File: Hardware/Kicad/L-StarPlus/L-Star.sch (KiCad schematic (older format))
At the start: 51 parts, among them IC1 24LC512, IC2 AS6C1008-55PCN, IC3 WDC 65C02, IC4 P8X32A, IC5 LM1086-5.0, IC6 LM1086-3.3, P1 PROP PLUG, P2 EXPANSION, P3 PS/2 KBD, P4 RESET, P5 RESET6502, P6 VIDEO OUT, P7 7-15V 1-1.5A IN, SW1 RESET, SW2 RESET6502, SW3 OFF - ON, U1 OSHW Logo, U2 Mount hole, U3 Mount hole, U4 Mount hole, X1 5MHz

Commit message: Fixed jumpers, added Reset, moved LED
I inadvertently put ~RAMEN on the wrong jumper in Rev2 (J2 instead of J4) so it was impossible to have keyboard, video and SRAM. This moves ~RAMEN to J4 and A16 to J2.
Also added ~RESET6502 to the jumpers to make it possible to connect a Propeller pin to it
There was not enough space around the RESET6502 button in Rev2 so I moved the LED to make space. I also moved both pushbutton switches to be parallel and centered between surrounding parts.
Also some more minor modifications to PCB and schematic.
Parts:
- IC3: value WDC 65C02 -> W65C02S6TPG-14
- JP1, JP3, JP5: footprint Pin_Headers:Pin_Header_Straight_1x07 -> 00Jac:00JG-Pin_Header_Straight_1x08; symbol CONN_01X07 -> CONN_01X08
- JP2: value RDY/~SO~/~SYNC~/~NMI~/~IRQ~/~RAMEN~/+ -> RDY/~SO~/~SYNC~/~NMI~/~IRQ~/~RES~/A16/GND; footprint Pin_Headers:Pin_Header_Straight_1x07 -> 00Jac:00JG-Pin_Header_Straight_1x08; symbol CONN_01X07 -> CONN_01X08
- JP4: value RDY/~SO~/~SYNC~/~NMI~/~IRQ~/A16/GND -> RDY/~SO~/~SYNC~/~NMI~/~IRQ~/~RES~/~RAM~/+3.3; footprint Pin_Headers:Pin_Header_Straight_1x07 -> 00Jac:00JG-Pin_Header_Straight_1x08; symbol CONN_01X07 -> CONN_01X08
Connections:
- net +3V3: now also JP4.1 (P1); no longer JP2.1 (P1)
- net A16: now also JP2.2 (P2); no longer JP4.2 (P2)
- net GND: now also JP2.1 (P1); no longer JP4.1 (P1)
- net P25: now also JP1.8 (P8)
- net P26: now also JP3.8 (P8)
- net P27: now also JP5.8 (P8)
- net RDY: now also JP2.8 (P8), JP4.8 (P8); no longer JP2.7 (P7), JP4.7 (P7)
- net ~IRQ: now also JP2.4 (P4), JP4.4 (P4); no longer JP2.3 (P3), JP4.3 (P3)
- net ~NMI: now also JP2.5 (P5), JP4.5 (P5); no longer JP2.4 (P4), JP4.4 (P4)
- net ~RAMEN: now also JP4.2 (P2); no longer JP2.2 (P2)
- net ~RES6502: now also JP2.3 (P3), JP4.3 (P3)
- net ~SO: now also JP2.7 (P7), JP4.7 (P7); no longer JP2.6 (P6), JP4.6 (P6)
- net ~SYNC: now also JP2.6 (P6), JP4.6 (P6); no longer JP2.5 (P5), JP4.5 (P5)

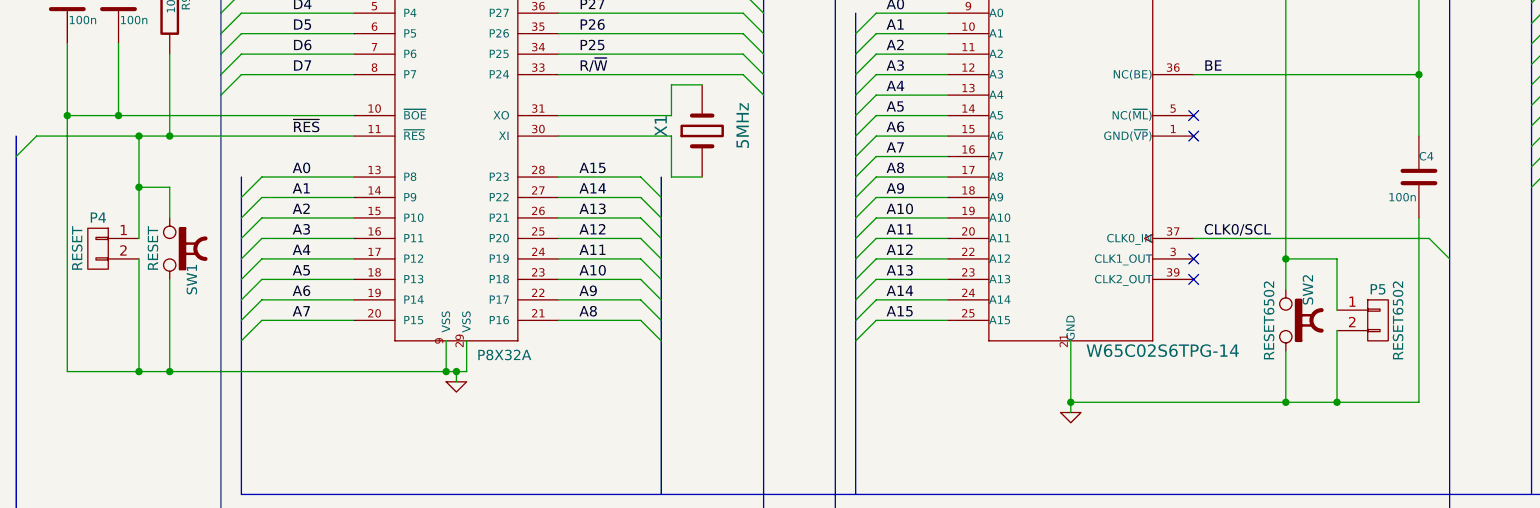
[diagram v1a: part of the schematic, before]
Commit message: Rev 3 Finished
Made all the soldering pads a little bigger, and made the pads for the voltage regulators a little smaller to leave more room for the switch. Many more small tweaks to footprints and PCB.
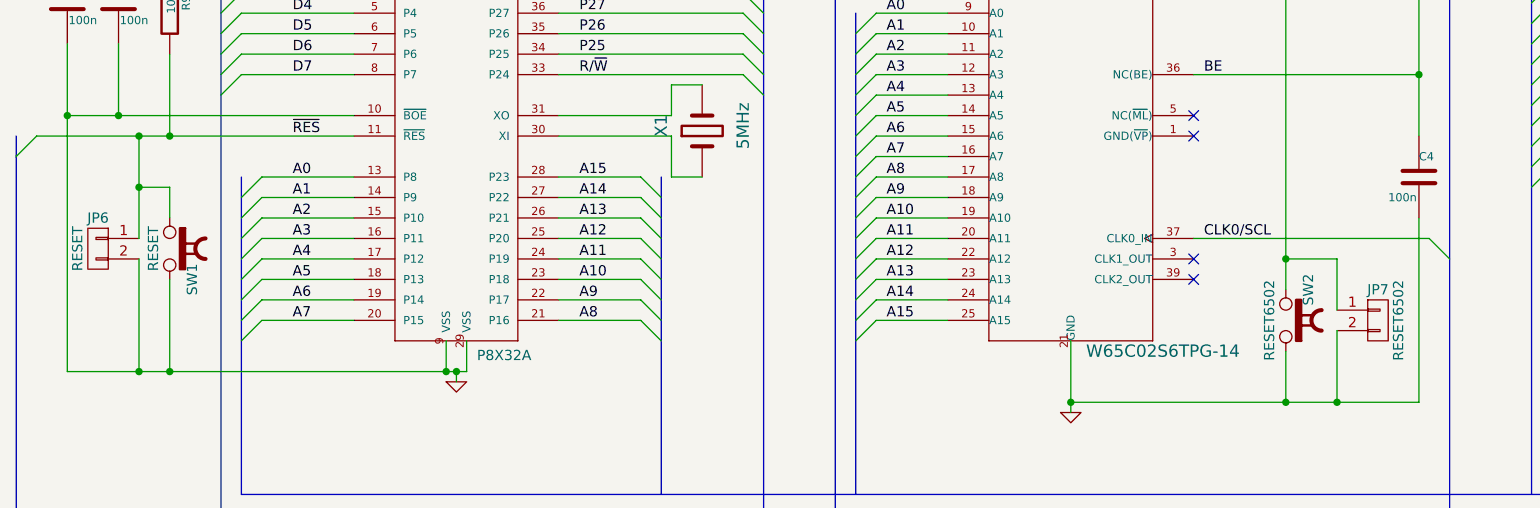
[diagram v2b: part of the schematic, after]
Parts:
- C7, C8, C9: footprint Discret:C1V7 -> 00Jac:00JG-C1V5
- IC1: footprint Sockets_DIP:DIP-8__300 -> 00Jac:00JG-DIP-8__300
- IC2: footprint Sockets_DIP:DIP-32__600 -> 00Jac:00JG-DIP-32__600
- IC3, IC4: footprint Sockets_DIP:DIP-40__600 -> 00Jac:00JG-DIP-40__600
- JP6: renamed from P4; footprint Pin_Headers:Pin_Header_Straight_1x02 -> 00Jac:00JG-Pin_Header_Straight_1x02
- JP7: renamed from P5; footprint Pin_Headers:Pin_Header_Straight_1x02 -> 00Jac:00JG-Pin_Header_Straight_1x02
- P1: footprint Pin_Headers:Pin_Header_Angled_1x04 -> 00Jac:00JG-Pin_Header_Angled_1x04
- P2: footprint Pin_Headers:Pin_Header_Straight_2x20 -> 00Jac:00JG-Pin_Header_Straight_2x20
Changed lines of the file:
@@
 F 0 "P1" V 12750 4300 50  0000 C CNN
 F 1 "PROP PLUG" V 12950 4300 50  0000 C CNN
-F 2 "Pin_Headers:Pin_Header_Angled_1x04" H 12800 4300 60  0001 C CNN
+F 2 "00Jac:00JG-Pin_Header_Angled_1x04" H 12800 4300 60  0001 C CNN
 F 3 "~" H 12800 4300 60  0000 C CNN
 	1    12800 4300
@@
 F 0 "C7" H 5250 9400 50  0000 L CNN
 F 1 "47u/16V" H 5250 9150 50  0000 L CNN
-F 2 "Discret:C1V7" H 5200 9300 60  0001 C CNN
+F 2 "00Jac:00JG-C1V5" H 5200 9300 60  0001 C CNN
 F 3 "~" H 5200 9300 60  0000 C CNN
 	1    5200 9300
@@
 F 0 "C8" H 6150 9400 50  0000 L CNN
 F 1 "47u/16V" H 6150 9150 50  0000 L CNN
-F 2 "Discret:C1V7" H 6100 9300 60  0001 C CNN
+F 2 "00Jac:00JG-C1V5" H 6100 9300 60  0001 C CNN
 F 3 "~" H 6100 9300 60  0000 C CNN
 	1    6100 9300
@@
 F 0 "C9" H 7050 9400 50  0000 L CNN
 F 1 "47u/16V" H 7050 9150 50  0000 L CNN
-F 2 "Discret:C1V7" H 7000 9300 60  0001 C CNN
+F 2 "00Jac:00JG-C1V5" H 7000 9300 60  0001 C CNN
 F 3 "~" H 7000 9300 60  0000 C CNN
 	1    7000 9300
@@
 F 0 "IC4" H 2650 6650 50  0000 L BNN
 F 1 "P8X32A" H 3050 4400 50  0000 L BNN
-F 2 "Sockets_DIP:DIP-40__600" H 2950 5550 50  0001 C CNN
+F 2 "00Jac:00JG-DIP-40__600" H 2950 5550 50  0001 C CNN
 F 3 "~" H 3100 5300 60  0000 C CNN
 	1    2950 5550
@@
 F 0 "IC1" H 2750 3000 60  0000 C CNN
 F 1 "24LC512" H 3150 2300 60  0000 C CNN
-F 2 "Sockets_DIP:DIP-8__300" H 2950 2650 60  0001 C CNN
+F 2 "00Jac:00JG-DIP-8__300" H 2950 2650 60  0001 C CNN
 F 3 "" H 2950 2650 60  0000 C CNN
 	1    2950 2650
@@
 F 0 "IC3" H 5600 6650 60  0000 C CNN
 F 1 "W65C02S6TPG-14" H 6400 3950 60  0000 C CNN
-F 2 "Sockets_DIP:DIP-40__600" H 5250 6850 60  0001 C CNN
+F 2 "00Jac:00JG-DIP-40__600" H 5250 6850 60  0001 C CNN
 F 3 "~" H 5950 5300 60  0000 C CNN
 	1    5950 5300
@@
 F 0 "IC2" H 8750 5875 50  0000 L BNN
 F 1 "AS6C1008-55PCN" H 8400 3950 50  0000 L BNN
-F 2 "Sockets_DIP:DIP-32__600" H 9150 4950 50  0001 C CNN
+F 2 "00Jac:00JG-DIP-32__600" H 9150 4950 50  0001 C CNN
 F 3 "" H 9150 4950 60  0000 C CNN
 	1    9150 4950
@@
 F 0 "P2" H 14500 6450 50  0000 C CNN
 F 1 "EXPANSION" V 14500 5400 50  0000 C CNN
-F 2 "Pin_Headers:Pin_Header_Straight_2x20" H 14500 4450 60  0001 C CNN
+F 2 "00Jac:00JG-Pin_Header_Straight_2x20" H 14500 4450 60  0001 C CNN
 F 3 "" H 14500 4450 60  0000 C CNN
 	1    14500 5400
@@
 $EndComp
 $Comp
-L CONN_01X02 P5
+L CONN_01X02 JP7
 U 1 1 54CD3D2C
 P 7450 6500
-F 0 "P5" H 7450 6650 50  0000 C CNN
+F 0 "JP7" H 7450 6650 50  0000 C CNN
 F 1 "RESET6502" V 7550 6500 50  0000 C CNN
-F 2 "Pin_Headers:Pin_Header_Straight_1x02" H 7450 6500 60  0001 C CNN
+F 2 "00Jac:00JG-Pin_Header_Straight_1x02" H 7450 6500 60  0001 C CNN
 F 3 "" H 7450 6500 60  0000 C CNN
 	1    7450 6500
@@
 $EndComp
 $Comp
-L CONN_01X02 P4
+L CONN_01X02 JP6
 U 1 1 54CD4BD6
 P 1200 6150
-F 0 "P4" H 1200 6300 50  0000 C CNN
+F 0 "JP6" H 1200 6300 50  0000 C CNN
 F 1 "RESET" V 1300 6150 50  0000 C CNN
-F 2 "Pin_Headers:Pin_Header_Straight_1x02" H 1200 6150 60  0001 C CNN
+F 2 "00Jac:00JG-Pin_Header_Straight_1x02" H 1200 6150 60  0001 C CNN
 F 3 "" H 1200 6150 60  0000 C CNN
 	1    1200 6150

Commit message: Rev.4 schematic and PCB
Replaced the expansion connector by a 50-pin header so I could add all the signals including BE (I added a pull-up resistor for the BE pin). It's even possible to replicate the entire jumper block on an expension board or an external connector now. Another possibility is to cut off the entire right side of the board (with all the connections and the jumper block) or leave it unpopulated, and make the necessary connections via the expansion port. The new connector is backwards compatible with the old one from the Rev.1, Rev.2 and Rev.3 boards.

Rewired almost the entire board to make it smaller again; I finally got it to fit into slightly over 80x100mm (you'll have to cut a small sliver off the top or bottom to make it fit completely)

For this, I slightly reduced the size of the TO220 pads for the voltage regulators.

Also fixed a small problem in the mini-din 6 footprint: the shield is now grounded.
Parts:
- added R16: 3K3, 00Jac:00JG-R400, symbol R
- P2: footprint 00Jac:00JG-Pin_Header_Straight_2x20 -> Pin_Headers:Pin_Header_Straight_2x25; symbol CONN_02X20 -> CONN_02X25
- P7: value 7-15V 1-1.5A IN -> 7-15V 1.5A IN
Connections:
- net +3V3: now also P2.9 (P9), R16.1; no longer IC3.36 (NC(BE)), P2.1 (P1)
- net +5V: now also P2.11 (P11); no longer P2.3 (P3)
- net A0: now also P2.33 (P33); no longer P2.25 (P25)
- net A1: now also P2.35 (P35); no longer P2.27 (P27)
- net A10: now also IC2.27 (A8), P2.44 (P44); no longer IC2.28 (A13), P2.36 (P36)
- net A11: now also IC2.28 (A13), P2.42 (P42); no longer IC2.23 (A10), P2.34 (P34)
- net A12: now also IC2.26 (A9), P2.40 (P40); no longer IC2.27 (A8), P2.32 (P32)
- net A13: now also IC2.25 (A11), P2.38 (P38); no longer IC2.26 (A9), P2.30 (P30)
- net A14: now also IC2.23 (A10), P2.36 (P36); no longer IC2.25 (A11), P2.28 (P28)
- net A15: now also P2.34 (P34); no longer P2.26 (P26)
- net A16: now also P2.1 (P1)
- net A2: now also P2.37 (P37); no longer P2.29 (P29)
- net A3: now also P2.39 (P39); no longer P2.31 (P31)
- net A4: now also P2.41 (P41); no longer P2.33 (P33)
- net A5: now also P2.43 (P43); no longer P2.35 (P35)
- net A6: now also P2.45 (P45); no longer P2.37 (P37)
- net A7: now also P2.47 (P47); no longer P2.39 (P39)
- net A8: now also P2.48 (P48); no longer P2.40 (P40)
- net A9: now also P2.46 (P46); no longer P2.38 (P38)
- net CLK0/SCL: now also P2.24 (P24); no longer P2.16 (P16)
- net D0: now also P2.17 (P17); no longer P2.9 (P9)
- net D1: now also IC2.14 (DQ1), P2.19 (P19); no longer IC2.17 (DQ3), P2.11 (P11)
- net D2: now also IC2.13 (DQ0), P2.21 (P21); no longer IC2.14 (DQ1), P2.13 (P13)
- net D3: now also IC2.17 (DQ3), P2.23 (P23); no longer IC2.13 (DQ0), P2.15 (P15)
- net D4: now also P2.25 (P25); no longer P2.17 (P17)
- net D5: now also P2.27 (P27); no longer P2.19 (P19)
- net D6: now also P2.29 (P29); no longer P2.21 (P21)
- net D7: now also P2.31 (P31); no longer P2.23 (P23)
- net GND: now also P2.10 (P10), P2.49 (P49), P2.50 (P50); no longer P2.2 (P2)
- net KBCLK: now also P2.4 (P4)
- net KBDATA: now also P2.6 (P6)
- net P25: now also P2.30 (P30); no longer P2.22 (P22)
- net P26: now also P2.28 (P28); no longer P2.20 (P20)
- net P27: now also P2.26 (P26); no longer P2.18 (P18)
- net P30: now also P2.20 (P20); no longer P2.12 (P12)
- net P31: now also P2.18 (P18); no longer P2.10 (P10)
- net R/~W: now also P2.32 (P32); no longer P2.24 (P24)
- net RDY: now also P2.7 (P7)
- net SDA: now also P2.22 (P22); no longer P2.14 (P14)
- net TVOUT: now also P2.8 (P8)
- net ~IRQ: now also P2.14 (P14); no longer P2.6 (P6)
- net ~NMI: now also P2.13 (P13); no longer P2.5 (P5)
- net ~RAMEN: now also P2.3 (P3)
- net ~RES: now also P2.2 (P2)
- net ~RES6502: now also P2.12 (P12); no longer P2.4 (P4)
- net ~SO: now also P2.15 (P15); no longer P2.7 (P7)
- net ~SYNC: now also P2.16 (P16); no longer P2.8 (P8)
- new net BE: IC3.36 (NC(BE)), P2.5 (P5), R16.2
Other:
- moved on the sheet: C6

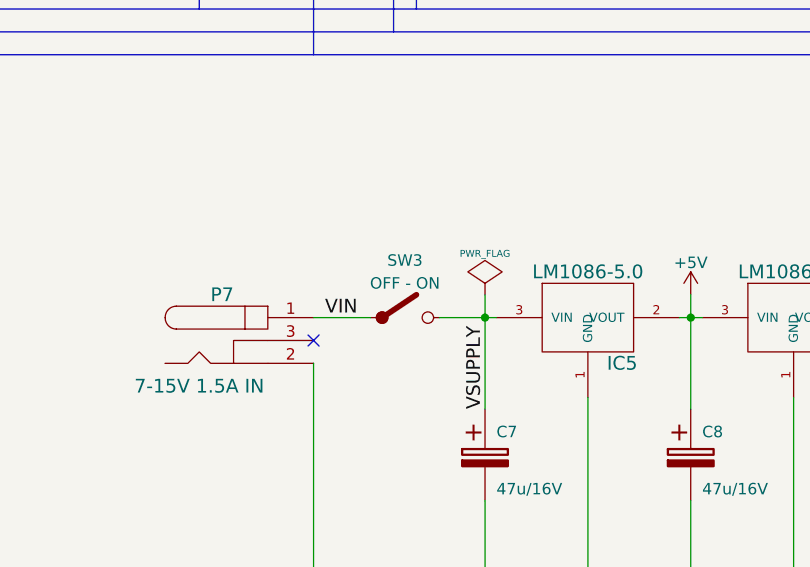
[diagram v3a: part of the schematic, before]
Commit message: PCB Revision 5
I had Rev 4 manufactured at OSHPark and ran into the following problems:
1. The pad-to-soldermask clearance was too big (.0078 inches) so the copper of the flood planes was exposed
2. The flood plane clearance was too small so in combination with the above, it was too easy to short pads to flood planes
3. In a few places, parts were too close together, which also made it too easy to cause short circuits
4. Some vias didn't get drilled because apparently the drill bit broke while the factory was processing my board
5. I had moved the mounting hole on the bottom left under the SRAM chip but that really wasn't a good location

To fix this, I made the following changes:
- Changed the pad-to-soldermask clearance to .002 inches (advised by James Neal from OSHPark)
- Changed the flood plane clearance to .01 inches and the minimum width to .006 inches (matching OSHPark specifications)
- Changed all the vias in the default net class to increase them in size by .005; hopefully a bigger drill is less likely to break
- Moved some parts slightly (e.g. the PS/2 connector) to make it less likely that a soldering mishap shorts out the board
- Swapped the locations of the on-off switch and the power connector, and moved the SRAM chip up a little to provide enough space to put the bottom left mounting hole on the corner.
- Some other minor tweaks
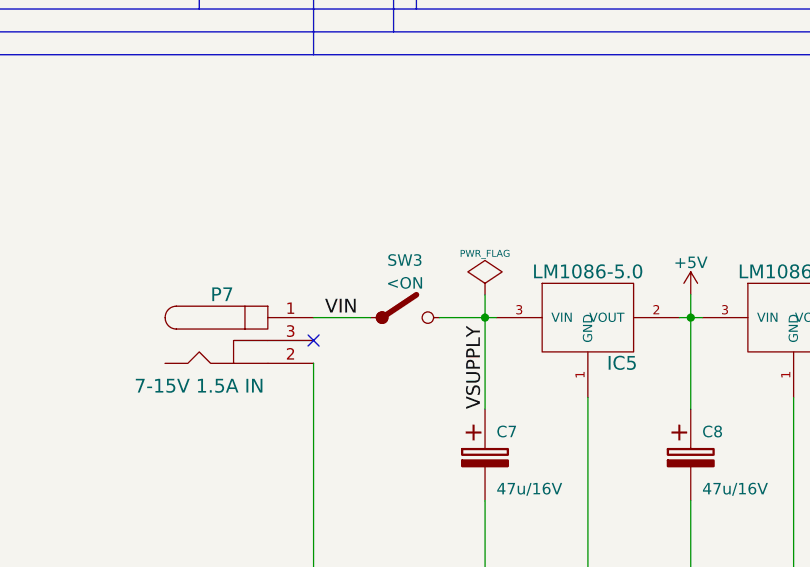
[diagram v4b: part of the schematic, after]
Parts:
- SW3: value OFF - ON -> <ON
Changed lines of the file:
@@
 Sheet 1 1
 Title "L-Star Simplified Software-Defined 6502 Computer Kit"
-Date "2016-08-28"
-Rev "4"
+Date "2016-10-07"
+Rev "5"
 Comp "(C) 2016 Jac Goudsmit"
 Comment1 "Open Source Hardware (MIT License)"
 Comment2 "https://github.com/JacGoudsmit/L-Star"
 Comment3 "https://hackaday.io/project/3620"
-Comment4 ""
+Comment4 "https://l-star.org"
 $EndDescr
 $Comp
@@
 Text Label 8300 5550 0    60   ~ 0
 A9
-Text Label 8300 5450 0    60   ~ 0
-A11
 Text Label 8300 5350 0    60   ~ 0
 A8
@@
 P 4850 8700
 F 0 "SW3" H 4850 8950 50  0000 C CNN
-F 1 "OFF - ON" H 4850 8850 50  0000 C CNN
+F 1 "<ON" H 4850 8850 50  0000 C CNN
 F 2 "00Jac:00JG-NKK_CS12ANW03" H 4850 8850 50  0001 C CNN
 F 3 "" H 4850 8700 60  0000 C CNN
@@
 Wire Wire Line
 	12350 6800 12450 6800
+Text Label 8300 5450 0    60   ~ 0
+A11
 $EndSCHEMATC
